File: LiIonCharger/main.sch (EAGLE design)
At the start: 8 parts, among them IC1 MCP73831

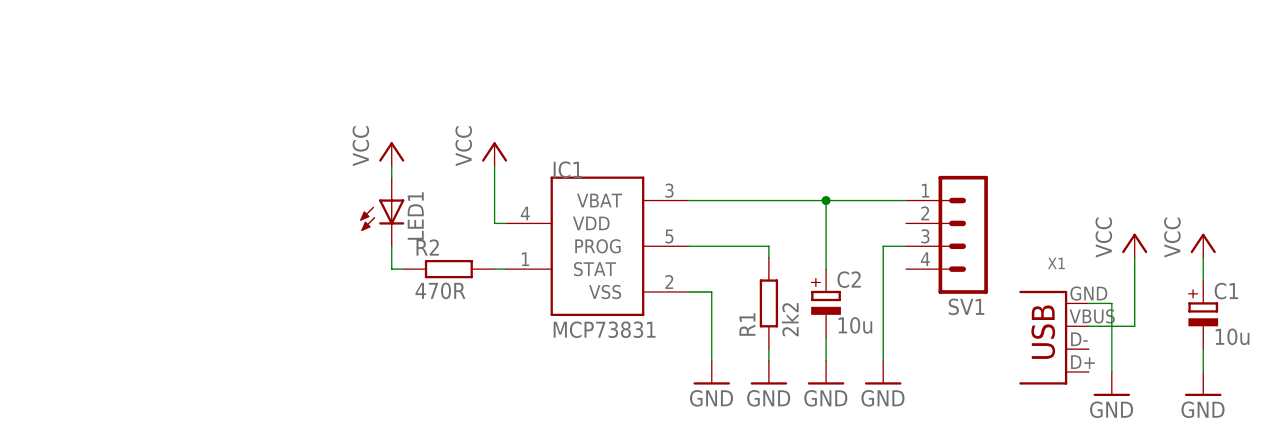
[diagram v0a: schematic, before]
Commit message: Fixed to be only on one layer.
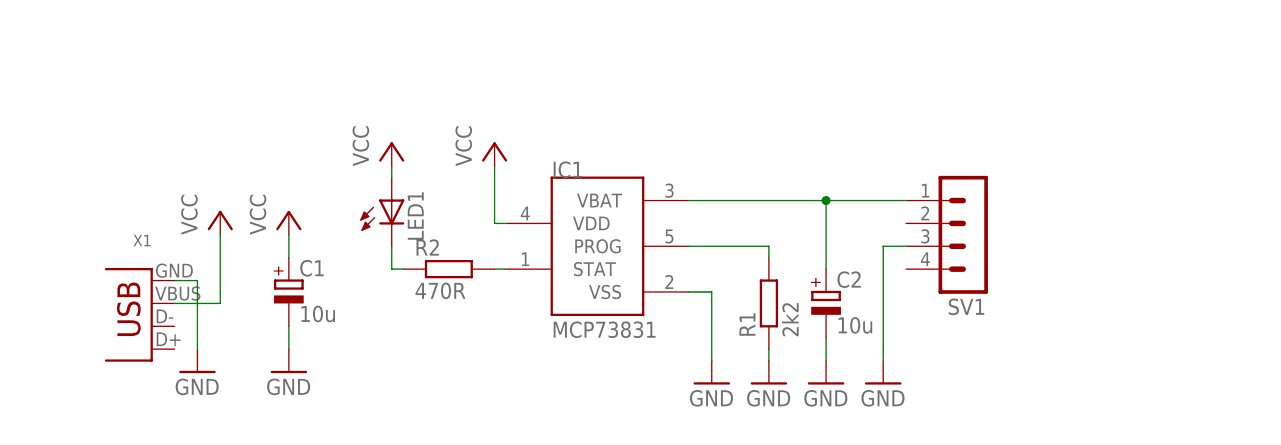
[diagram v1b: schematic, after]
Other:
- moved on the sheet: C1, X1
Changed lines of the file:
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@@
 <setting verticaltext="up"/>
 </settings>
-<grid distance="50" unitdist="mil" unit="mil" style="lines" multiple="1" display="yes" altdistance="0.01" altunitdist="inch" altunit="inch"/>
+<grid distance="0.05" unitdist="inch" unit="inch" style="lines" multiple="1" display="yes" altdistance="0.01" altunitdist="inch" altunit="inch"/>
 <layers>
 <layer number="1" name="Top" color="4" fill="1" visible="no" active="no"/>
@@
 <instance part="P+2" gate="VCC" x="-13.97" y="59.69"/>
 <instance part="GND1" gate="1" x="10.16" y="33.02"/>
-<instance part="C1" gate="G$1" x="64.77" y="41.91"/>
+<instance part="C1" gate="G$1" x="-36.83" y="44.45"/>
 <instance part="C2" gate="G$1" x="22.86" y="43.18"/>
-<instance part="P+3" gate="VCC" x="64.77" y="49.53"/>
-<instance part="GND3" gate="1" x="64.77" y="31.75"/>
+<instance part="P+3" gate="VCC" x="-36.83" y="52.07"/>
+<instance part="GND3" gate="1" x="-36.83" y="34.29"/>
 <instance part="GND4" gate="1" x="22.86" y="33.02"/>
 <instance part="SV1" gate="1" x="39.37" y="48.26" rot="R180"/>
 <instance part="GND5" gate="1" x="29.21" y="33.02"/>
-<instance part="X1" gate="G$1" x="49.53" y="41.91" rot="R180"/>
-<instance part="P+4" gate="VCC" x="57.15" y="49.53"/>
-<instance part="GND6" gate="1" x="54.61" y="31.75"/>
+<instance part="X1" gate="G$1" x="-52.07" y="44.45" rot="R180"/>
+<instance part="P+4" gate="VCC" x="-44.45" y="52.07"/>
+<instance part="GND6" gate="1" x="-46.99" y="34.29"/>
 </instances>
 <busses>
@@
 <pinref part="C1" gate="G$1" pin="-"/>
 <pinref part="GND3" gate="1" pin="GND"/>
-<wire x1="64.77" y1="36.83" x2="64.77" y2="34.29" width="0.1524" layer="91"/>
+<wire x1="-36.83" y1="39.37" x2="-36.83" y2="36.83" width="0.1524" layer="91"/>
 </segment>
 <segment>
@@
 <pinref part="X1" gate="G$1" pin="GND"/>
 <pinref part="GND6" gate="1" pin="GND"/>
-<wire x1="52.07" y1="41.91" x2="54.61" y2="41.91" width="0.1524" layer="91"/>
-<wire x1="54.61" y1="41.91" x2="54.61" y2="34.29" width="0.1524" layer="91"/>
+<wire x1="-49.53" y1="44.45" x2="-46.99" y2="44.45" width="0.1524" layer="91"/>
+<wire x1="-46.99" y1="44.45" x2="-46.99" y2="36.83" width="0.1524" layer="91"/>
 </segment>
 </net>
@@
 <pinref part="P+3" gate="VCC" pin="VCC"/>
 <pinref part="C1" gate="G$1" pin="+"/>
-<wire x1="64.77" y1="46.99" x2="64.77" y2="44.45" width="0.1524" layer="91"/>
+<wire x1="-36.83" y1="49.53" x2="-36.83" y2="46.99" width="0.1524" layer="91"/>
 </segment>
 <segment>
 <pinref part="X1" gate="G$1" pin="VBUS"/>
 <pinref part="P+4" gate="VCC" pin="VCC"/>
-<wire x1="52.07" y1="39.37" x2="57.15" y2="39.37" width="0.1524" layer="91"/>
-<wire x1="57.15" y1="39.37" x2="57.15" y2="46.99" width="0.1524" layer="91"/>
+<wire x1="-49.53" y1="41.91" x2="-44.45" y2="41.91" width="0.1524" layer="91"/>
+<wire x1="-44.45" y1="41.91" x2="-44.45" y2="49.53" width="0.1524" layer="91"/>
 </segment>
 </net>

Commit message: 7 Segment LED Display project added.
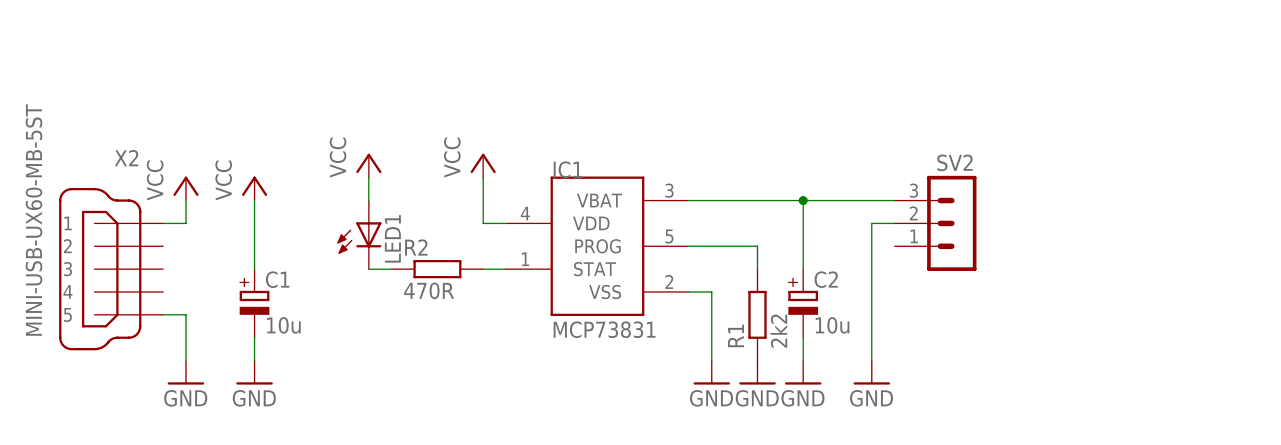
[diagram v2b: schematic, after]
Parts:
- removed SV1: (no value), con-lstb:MA04-1
- removed X1: (no value), con-usb-3:USB-A-H
- added SV2: (no value), con-lstb:MA03-1
- added X2: MINI-USB-UX60-MB-5ST, con-hirose:MINI-USB-UX60-MB-5ST
- LED1: device led:LED5MM -> led:LEDSML0805
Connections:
- net GND: now also SV2.2, X2.5; no longer SV1.3, X1.GND
- net N$4: now also SV2.3; no longer SV1.1
- net VCC: now also X2.1; no longer X1.VBUS
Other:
- moved on the sheet: C1, C2, LED1, R1, R2
